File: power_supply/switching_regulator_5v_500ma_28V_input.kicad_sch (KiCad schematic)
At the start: 9 parts, among them U1 R-78E5.0-0.5

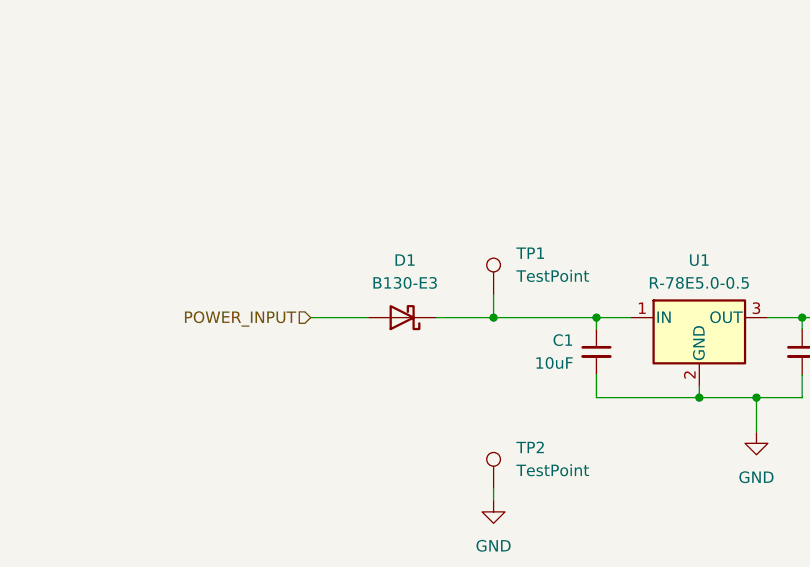
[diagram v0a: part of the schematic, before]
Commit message: changed RP diode
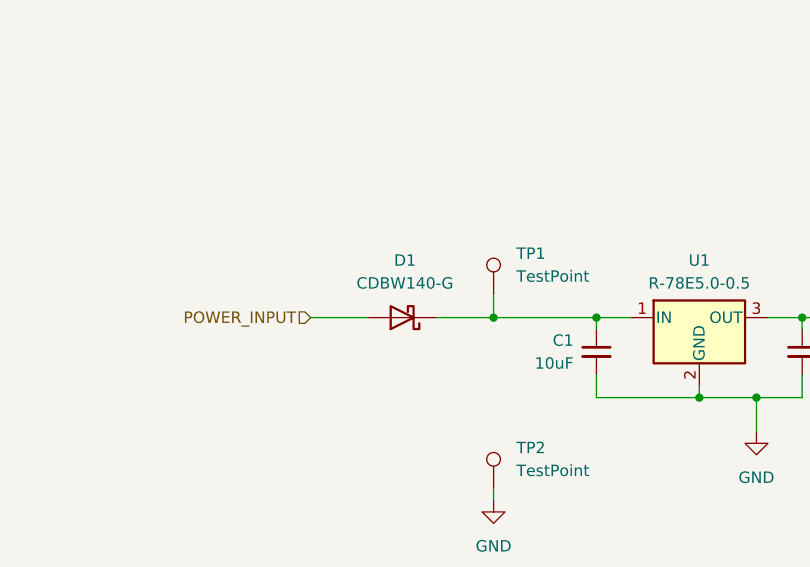
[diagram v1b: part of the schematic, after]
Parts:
- D1: value B130-E3 -> CDBW140-G
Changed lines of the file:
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@@
 			)
 		)
-		(property "Value" "B130-E3"
+		(property "Value" "CDBW140-G"
 			(at 115.8875 83.82 0)
 			(effects
